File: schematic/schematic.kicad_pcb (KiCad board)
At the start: 4 copper layers, 100 x 100 mm, 262 parts, among them J1 Conn_01x04, J10 Conn_01x03, J11 Conn_01x02, J12 Conn_01x02, J13 Conn_01x02, J14 Conn_01x02, J15 Conn_01x02, J16 Conn_01x02, J17 Conn_01x04, J18 Conn_02x13_Odd_Even, J19 Conn_02x05_Odd_Even, J2 Conn_01x04, J20 Conn_02x05_Odd_Even, J3 Conn_01x04, J4 Conn_01x04, J5 Conn_01x04, J6 Conn_01x06, J7 Conn_01x03, J8 Screw_Terminal_01x02, J9 Conn_01x03, Q1 PSMN1R7-30YL, Q2 PSMN1R7-30YL, Q3 NCV8402, Q4 NCV8402, SW1 SW_Push_Dual, SW2 SW_DIP_x03, U1 STM32F401VETx, U2 TMC2130, U3 TMC2130, U4 TMC2130, U5 TMC2130, U6 BD9E302EFJ, U7 BD9E302EFJ, U8 BD9E302EFJ, Y1 Crystal_GND24

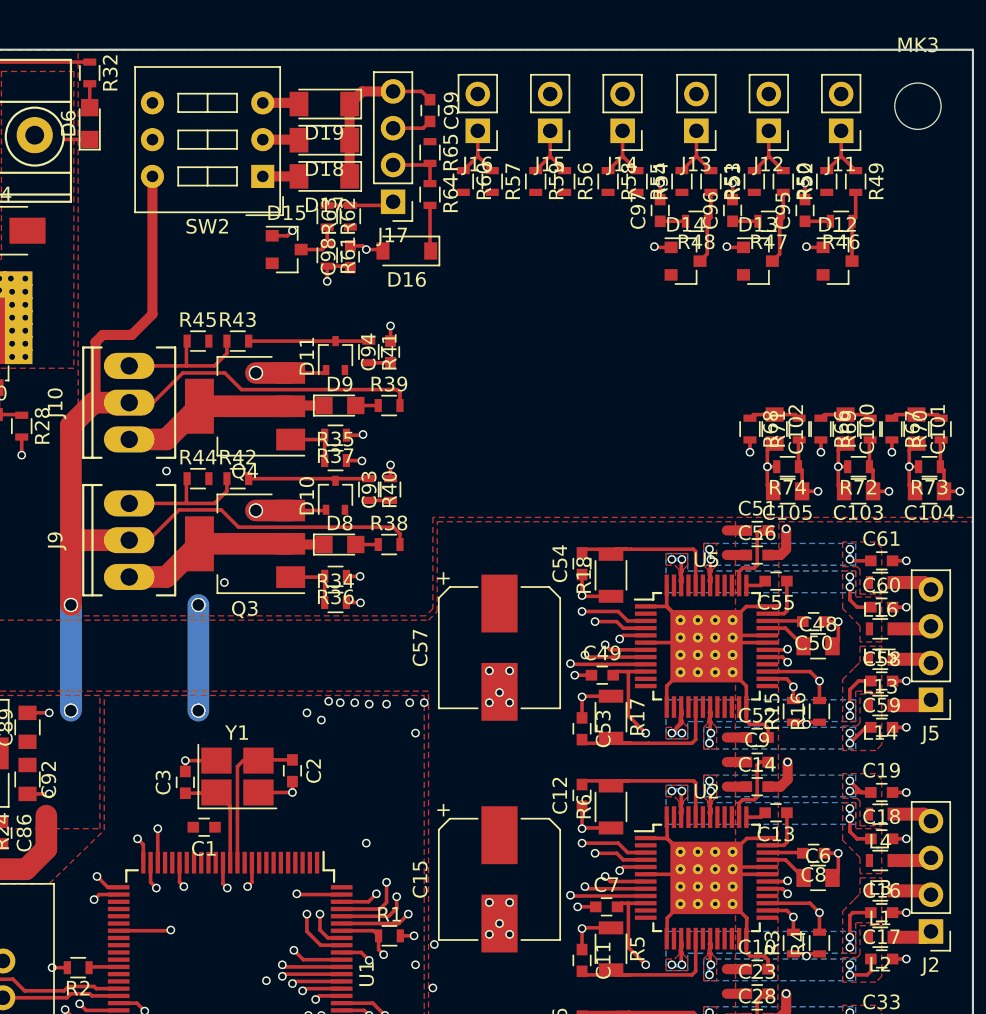
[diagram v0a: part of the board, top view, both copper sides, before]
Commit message: Routed thermal sensors
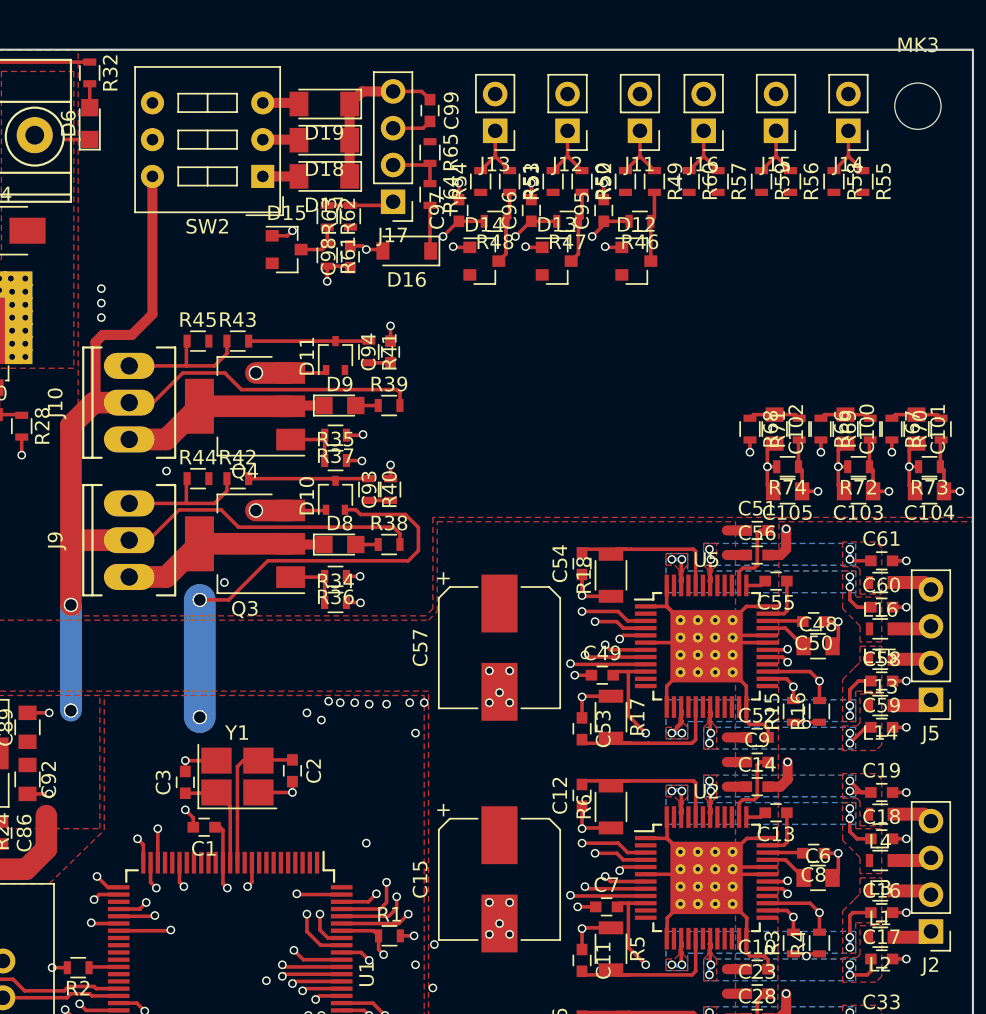
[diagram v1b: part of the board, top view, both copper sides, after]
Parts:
- moved J15 15.6 mm to (251.4, 55.6)
- moved J16 15.6 mm to (246.4, 55.6)
- moved R56 15.6 mm to (252.4, 59.1)
- moved R57 15.6 mm to (247.4, 59.1)
- moved R58 15.6 mm to (255.4, 59.1)
- moved R59 15.6 mm to (250.4, 59.1)
- moved R60 15.6 mm to (245.4, 59.1)
- moved J14 15.6 mm to (256.4, 55.6)
- moved R55 15.6 mm to (257.4, 59.1)
- moved C95 13.9 mm to (239.5, 61.1)
- moved C96 13.9 mm to (234.5, 61.1)
- moved C97 13.9 mm to (229.5, 61.1)
- moved D12 13.9 mm to (241.8, 64.6)
- moved D13 13.9 mm to (236.2, 64.6)
- moved D14 13.9 mm to (231.2, 64.6)
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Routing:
- net THERM0: track 1.75 -> 86.5 mm, vias 0 -> 3
- net THERM1: track 1.75 -> 85.0 mm, vias 0 -> 3
- net THERM2: track 1.75 -> 78.2 mm, vias 0 -> 3
- net +3V3: track 149.5 -> 181.3 mm, vias 12 -> 14
- net (no net): track 7.30 -> 0.00 mm, vias 2 -> 0
- net RST: track 57.9 -> 60.8 mm
- net GND: track 403.8 -> 405.2 mm, vias 131 -> 132

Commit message: Finished routing
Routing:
- net +5V: track 17.5 -> 105.9 mm, vias 0 -> 1
- net XEND: track 0.00 -> 78.2 mm, vias 0 -> 4
- net YEND: track 0.00 -> 72.9 mm, vias 0 -> 4
- net ZEND: track 0.00 -> 69.8 mm, vias 0 -> 4
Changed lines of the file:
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@@
   (general
     (links 850)
-    (no_connects 21)
+    (no_connects 16)
     (area 163.195238 48.325 267.04762 154.782382)
     (thickness 1.6)
     (drawings 4)
-    (tracks 2087)
+    (tracks 2140)
     (zones 0)
     (modules 262)
@@
   )
   (setup
-    (last_trace_width 0.25)
+    (last_trace_width 0.9)
     (user_trace_width 0.7)
     (user_trace_width 0.9)
@@
   (segment (start 240.2 125.15) (end 240.15 125.2) (width 0.25) (layer F.Cu) (net 8) (status 30))
   (segment (start 240.6 109.05) (end 240.45 109.2) (width 0.25) (layer F.Cu) (net 8) (status 30))
+  (via (at 262.2 84) (size 1) (drill 0.8) (layers F.Cu B.Cu) (net 9))
+  (segment (start 208.33 56.21) (end 213.64 50.9) (width 0.9) (layer In1.Cu) (net 9))
+  (segment (start 243.8 50.9) (end 213.64 50.9) (width 0.9) (layer In1.Cu) (net 9))
+  (segment (start 244.2 51.3) (end 243.8 50.9) (width 0.9) (layer In1.Cu) (net 9))
+  (segment (start 244.2 56.8) (end 244.2 51.3) (width 0.9) (layer In1.Cu) (net 9))
+  (segment (start 245.5 58.1) (end 244.2 56.8) (width 0.9) (layer In1.Cu) (net 9))
+  (segment (start 262.1 58.1) (end 245.5 58.1) (width 0.9) (layer In1.Cu) (net 9))
+  (segment (start 262.2 58) (end 262.1 58.1) (width 0.9) (layer In1.Cu) (net 9))
+  (segment (start 262.2 58) (end 262.2 84) (width 0.9) (layer In1.Cu) (net 9))
   (segment (start 195.84 137.64) (end 195.84 142.24) (width 0.9) (layer F.Cu) (net 9))
   (segment (start 195.84 142.24) (end 195.9 142.3) (width 0.9) (layer F.Cu) (net 9))
@@
   (segment (start 209.3 86.8) (end 209.3 79.1) (width 0.25) (layer In2.Cu) (net 147))
   (segment (start 207.3 88.8) (end 209.3 86.8) (width 0.25) (layer In2.Cu) (net 147))
+  (segment (start 228.05 70.4) (end 244 70.4) (width 0.25) (layer In1.Cu) (net 148))
+  (segment (start 227.9 102) (end 227.9 70.55) (width 0.25) (layer In2.Cu) (net 148))
+  (via (at 227.9 102) (size 0.6) (drill 0.4) (layers F.Cu B.Cu) (net 148))
+  (segment (start 227.9 102) (end 220.65 102) (width 0.25) (layer In1.Cu) (net 148))
+  (segment (start 227.9 70.55) (end 228.05 70.4) (width 0.25) (layer In2.Cu) (net 148))
+  (via (at 228.05 70.4) (size 0.6) (drill 0.4) (layers F.Cu B.Cu) (net 148))
+  (segment (start 218.7 106.15) (end 218.7 103.95) (width 0.25) (layer F.Cu) (net 148))
+  (segment (start 218.7 103.95) (end 220.65 102) (width 0.25) (layer F.Cu) (net 148))
+  (via (at 220.65 102) (size 0.6) (drill 0.4) (layers F.Cu B.Cu) (net 148))
+  (via (at 257.4 60.9) (size 0.6) (drill 0.4) (layers F.Cu B.Cu) (net 148))
+  (segment (start 257.4 60.9) (end 257.4 59.85) (width 0.25) (layer F.Cu) (net 148))
+  (segment (start 256 62.3) (end 257.4 60.9) (width 0.25) (layer In1.Cu) (net 148))
+  (segment (start 252.1 62.3) (end 256 62.3) (width 0.25) (layer In1.Cu) (net 148))
+  (segment (start 244 70.4) (end 252.1 62.3) (width 0.25) (layer In1.Cu) (net 148))
+  (segment (start 252.4 60.9) (end 243.6 69.7) (width 0.25) (layer In1.Cu) (net 149))
+  (segment (start 228.75 69.7) (end 228.8 69.65) (width 0.25) (layer In2.Cu) (net 149))
+  (via (at 228.8 69.65) (size 0.6) (drill 0.4) (layers F.Cu B.Cu) (net 149))
+  (segment (start 220.65 103.15) (end 227.65 103.15) (width 0.25) (layer In1.Cu) (net 149))
+  (segment (start 219.2 104.6) (end 220.65 103.15) (width 0.25) (layer F.Cu) (net 149))
+  (via (at 220.65 103.15) (size 0.6) (drill 0.4) (layers F.Cu B.Cu) (net 149))
+  (segment (start 219.2 106.15) (end 219.2 104.6) (width 0.25) (layer F.Cu) (net 149))
+  (via (at 228.75 102.05) (size 0.6) (drill 0.4) (layers F.Cu B.Cu) (net 149))
+  (segment (start 227.65 103.15) (end 228.75 102.05) (width 0.25) (layer In1.Cu) (net 149))
+  (segment (start 228.75 102.05) (end 228.75 69.7) (width 0.25) (layer In2.Cu) (net 149))
+  (via (at 252.4 60.9) (size 0.6) (drill 0.4) (layers F.Cu B.Cu) (net 149))
+  (segment (start 252.4 60.9) (end 252.4 59.85) (width 0.25) (layer F.Cu) (net 149))
+  (segment (start 228.85 69.7) (end 228.8 69.65) (width 0.25) (layer In1.Cu) (net 149))
+  (segment (start 243.6 69.7) (end 228.85 69.7) (width 0.25) (layer In1.Cu) (net 149))
+  (segment (start 247.4 59.85) (end 247.4 60.8) (width 0.25) (layer F.Cu) (net 150))
+  (segment (start 243.25 68.85) (end 247.4 64.7) (width 0.25) (layer In1.Cu) (net 150))
+  (segment (start 247.4 64.7) (end 247.4 60.8) (width 0.25) (layer In1.Cu) (net 150))
+  (via (at 247.4 60.8) (size 0.6) (drill 0.4) (layers F.Cu B.Cu) (net 150))
+  (segment (start 229.75 102.05) (end 229.75 68.9) (width 0.25) (layer In2.Cu) (net 150))
+  (via (at 229.75 102.05) (size 0.6) (drill 0.4) (layers F.Cu B.Cu) (net 150))
+  (segment (start 220.65 104.05) (end 221.400002 104.05) (width 0.25) (layer In1.Cu) (net 150))
+  (segment (start 219.7 105) (end 220.65 104.05) (width 0.25) (layer F.Cu) (net 150))
+  (via (at 220.65 104.05) (size 0.6) (drill 0.4) (layers F.Cu B.Cu) (net 150))
+  (segment (start 219.7 105) (end 219.7 106.15) (width 0.25) (layer F.Cu) (net 150))
+  (segment (start 221.800002 103.65) (end 228.15 103.65) (width 0.25) (layer In1.Cu) (net 150))
+  (segment (start 221.400002 104.05) (end 221.800002 103.65) (width 0.25) (layer In1.Cu) (net 150))
+  (segment (start 229.75 102.05) (end 228.15 103.65) (width 0.25) (layer In1.Cu) (net 150))
+  (via (at 229.8 68.85) (size 0.6) (drill 0.4) (layers F.Cu B.Cu) (net 150))
+  (segment (start 229.75 68.9) (end 229.8 68.85) (width 0.25) (layer In2.Cu) (net 150))
+  (segment (start 229.8 68.85) (end 243.25 68.85) (width 0.25) (layer In1.Cu) (net 150))
   (segment (start 217.4 110.950002) (end 217.213604 110.950002) (width 0.25) (layer In2.Cu) (net 151))
   (segment (start 221.8 109.7) (end 220.549998 110.950002) (width 0.25) (layer In2.Cu) (net 151))
@@
       (pts
         (xy 180.1 87.8) (xy 180.7 88.4) (xy 187.4 88.4) (xy 188.4 89.4) (xy 227.4 89.4)
-        (xy 228 88.8) (xy 228 82.6) (xy 248.6 82.6) (xy 248.6 132) (xy 243.6 132)
+        (xy 228 88.8) (xy 228 82.6) (xy 248.6 82.6) (xy 248.6 132.9) (xy 243.6 132.9)
         (xy 243.6 146.3) (xy 223 146.3) (xy 223 131.4) (xy 227.4 131.4) (xy 227.4 94.3)
         (xy 173.1 94.3) (xy 173 79.3) (xy 180 79.3)

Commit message: Added GPIO header
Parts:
- added J21: Conn_02x05_Odd_Even, Pin_Headers:Pin_Header_Straight_2x05_Pitch2.54mm, F.Cu at (243.6, 74.0)
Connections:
- U1 pad 15: Net-(U1-Pad15) -> GP6
- U1 pad 16: Net-(U1-Pad16) -> GP7
- U1 pad 17: Net-(U1-Pad17) -> GP8
- U1 pad 4: ZSTOP -> GP1
- U1 pad 5: Net-(U1-Pad5) -> GP2
- U1 pad 7: Net-(U1-Pad7) -> GP3
- U1 pad 8: Net-(U1-Pad8) -> GP4
- U1 pad 9: Net-(U1-Pad9) -> GP5

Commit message: Route gpio header
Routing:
- net GP1: track 0.00 -> 49.2 mm, vias 0 -> 1
- net GP5: track 0.00 -> 48.9 mm, vias 0 -> 1
- net GP2: track 0.00 -> 48.4 mm, vias 0 -> 1
- net GP3: track 0.00 -> 47.5 mm, vias 0 -> 1
- net GP7: track 0.00 -> 45.9 mm, vias 0 -> 1
- net GP6: track 0.00 -> 45.6 mm, vias 0 -> 1
- net GP8: track 0.00 -> 43.7 mm, vias 0 -> 1
- net GP4: track 0.00 -> 43.1 mm, vias 0 -> 1
- net F0PWM: track 33.6 -> 33.8 mm, vias 3 -> 4

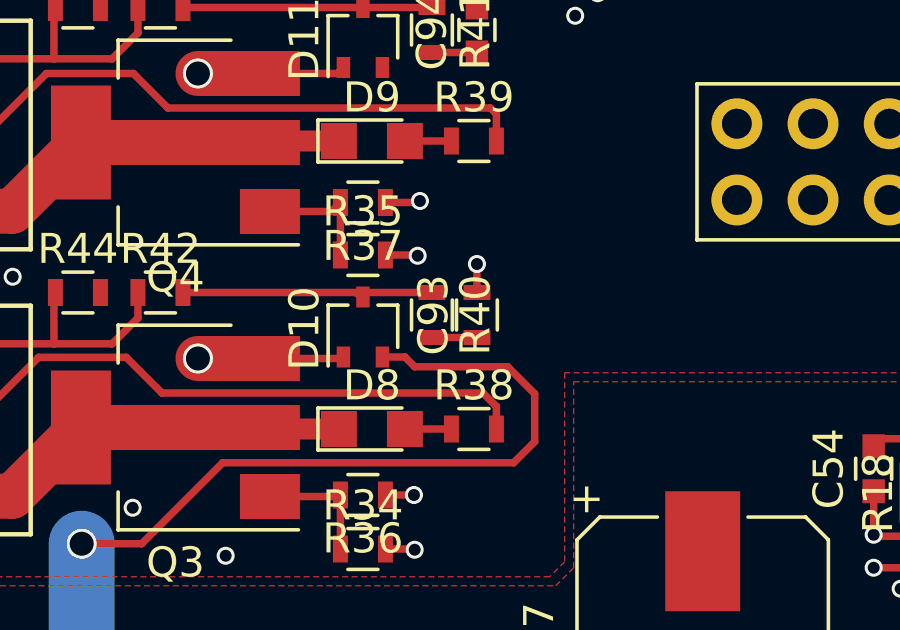
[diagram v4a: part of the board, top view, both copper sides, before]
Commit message: Fixed C93 footprint
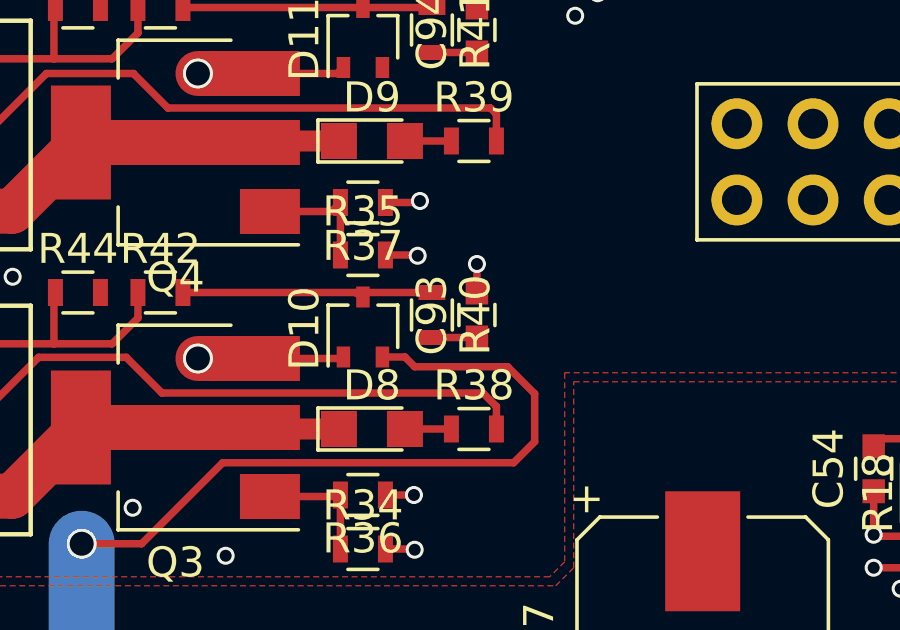
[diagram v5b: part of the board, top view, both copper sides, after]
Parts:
- C93: footprint Resistors_SMD:R_0603 -> Capacitors_SMD:C_0603
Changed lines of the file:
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@@
     )
   )
-  (module Resistors_SMD:R_0603 (layer F.Cu)
-    (at 224.775 80.375 90)
-    (descr "Resistor SMD 0603, reflow soldering, Vishay (see dcrcw.pdf)")
-    (tags "resistor 0603")
-    (attr smd)
-    (fp_text reference C93 (at 0 -1.45 90) (layer F.SilkS)
-      (effects (font (size 1 1) (thickness 0.15)))
-    )
-    (fp_text value 100nF (at 0 1.5 90) (layer F.Fab)
-      (effects (font (size 1 1) (thickness 0.15)))
-    )
-    (fp_text user %R (at 0 0 90) (layer F.Fab)
-      (effects (font (size 0.4 0.4) (thickness 0.075)))
-    )
-    (fp_line (start -0.8 0.4) (end -0.8 -0.4) (layer F.Fab) (width 0.1))
-    (fp_line (start 0.8 0.4) (end -0.8 0.4) (layer F.Fab) (width 0.1))
-    (fp_line (start 0.8 -0.4) (end 0.8 0.4) (layer F.Fab) (width 0.1))
-    (fp_line (start -0.8 -0.4) (end 0.8 -0.4) (layer F.Fab) (width 0.1))
-    (fp_line (start 0.5 0.68) (end -0.5 0.68) (layer F.SilkS) (width 0.12))
-    (fp_line (start -0.5 -0.68) (end 0.5 -0.68) (layer F.SilkS) (width 0.12))
-    (fp_line (start -1.25 -0.7) (end 1.25 -0.7) (layer F.CrtYd) (width 0.05))
-    (fp_line (start -1.25 -0.7) (end -1.25 0.7) (layer F.CrtYd) (width 0.05))
-    (fp_line (start 1.25 0.7) (end 1.25 -0.7) (layer F.CrtYd) (width 0.05))
-    (fp_line (start 1.25 0.7) (end -1.25 0.7) (layer F.CrtYd) (width 0.05))
-    (pad 1 smd rect (at -0.75 0 90) (size 0.5 0.9) (layers F.Cu F.Paste F.Mask)
-      (net 72 T0))
-    (pad 2 smd rect (at 0.75 0 90) (size 0.5 0.9) (layers F.Cu F.Paste F.Mask)
-      (net 1 GND))
-    (model ${KISYS3DMOD}/Resistors_SMD.3dshapes/R_0603.wrl
-      (at (xyz 0 0 0))
-      (scale (xyz 1 1 1))
-      (rotate (xyz 0 0 0))
-    )
-  )
   (module Capacitors_SMD:C_0603 (layer F.Cu)
     (at 224.775 70.875 90)
@@
       (at (xyz 0 0 0))
       (scale (xyz 1 1 1))
+      (rotate (xyz 0 0 0))
+    )
+  )
+  (module Capacitors_SMD:C_0603 (layer F.Cu)
+    (at 224.775 80.375 90)
+    (descr "Capacitor SMD 0603, reflow soldering, AVX (see smccp.pdf)")
+    (tags "capacitor 0603")
+    (attr smd)
+    (fp_text reference C93 (at 0 -1.5 90) (layer F.SilkS)
+      (effects (font (size 1 1) (thickness 0.15)))
+    )
+    (fp_text value 100nF (at 0 1.5 90) (layer F.Fab)
+      (effects (font (size 1 1) (thickness 0.15)))
+    )
+    (fp_line (start 1.4 0.65) (end -1.4 0.65) (layer F.CrtYd) (width 0.05))
+    (fp_line (start 1.4 0.65) (end 1.4 -0.65) (layer F.CrtYd) (width 0.05))
+    (fp_line (start -1.4 -0.65) (end -1.4 0.65) (layer F.CrtYd) (width 0.05))
+    (fp_line (start -1.4 -0.65) (end 1.4 -0.65) (layer F.CrtYd) (width 0.05))
+    (fp_line (start 0.35 0.6) (end -0.35 0.6) (layer F.SilkS) (width 0.12))
+    (fp_line (start -0.35 -0.6) (end 0.35 -0.6) (layer F.SilkS) (width 0.12))
+    (fp_line (start -0.8 -0.4) (end 0.8 -0.4) (layer F.Fab) (width 0.1))
+    (fp_line (start 0.8 -0.4) (end 0.8 0.4) (layer F.Fab) (width 0.1))
+    (fp_line (start 0.8 0.4) (end -0.8 0.4) (layer F.Fab) (width 0.1))
+    (fp_line (start -0.8 0.4) (end -0.8 -0.4) (layer F.Fab) (width 0.1))
+    (fp_text user %R (at 0 0 90) (layer F.Fab)
+      (effects (font (size 0.3 0.3) (thickness 0.075)))
+    )
+    (pad 2 smd rect (at 0.75 0 90) (size 0.8 0.75) (layers F.Cu F.Paste F.Mask)
+      (net 1 GND))
+    (pad 1 smd rect (at -0.75 0 90) (size 0.8 0.75) (layers F.Cu F.Paste F.Mask)
+      (net 72 T0))
+    (model Capacitors_SMD.3dshapes/C_0603.wrl
+      (at (xyz 0 0 0))
+      (scale (xyz 1 1 1))
